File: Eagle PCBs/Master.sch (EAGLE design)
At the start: 12 parts

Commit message: Master PCB WIP
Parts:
- removed C4: 22uF 16V, rcl:C-EU025-025X050
- removed LED, SLAVE_PWR: (no value), con-molex:KK-156-2
- removed LED_T: BD239, transistor-neu-to92:BD239
- removed SLAVE_DATA: (no value), con-molex:22-23-2061
- added R1: 120Ω, rcl:R-EU_0207/10
- added SLAVE: 212528-0801, SamacSys_Parts:212528-0801
- 5V-VRR: value 7805T -> L7805CV
- C1: value 220uF 16V -> 0.33uF
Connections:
- removed net 12VCC: 5V-VRR.VI, C1.1, C2.1, LED-1.S, PSU.2, SLAVE_PWR-1.S
- removed net LED_DIM: LED_T.B
- removed net LED_GND: LED-2.S, LED_T.C
- new net VDD: 5V-VRR.VO, C2.1, C3.1, MEGA-1.S
- net GND: now also SLAVE.7; no longer C4.2, LED_T.E, SLAVE_PWR-2.S
- net MEGA_P18: now also MEGA-5.S; no longer MEGA-4.S
- net MEGA_P19: now also MEGA-3.S; no longer MEGA-5.S
- net MEGA_P2: now also MEGA-4.S; no longer MEGA-3.S
- net RS485_A: now also R1.2, SLAVE.3; no longer SLAVE_DATA-1.S
- net RS485_B: now also R1.1, SLAVE.4; no longer SLAVE_DATA-2.S
- net VCC: now also 5V-VRR.VI, C1.1, PSU.2, SLAVE.8; no longer 5V-VRR.VO, C3.1, C4.1, MEGA-1.S
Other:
- note added: "12 to 5V, 1.5A"
- note added: "Arduino Mega Connection"
- note added: "Slave Connection"
- note removed: "12 to 5V, 1A https://www.eleccircuit.com/12v-to-5v-converter-step-down-3a-regulator/"
- note removed: "Arduino Mega Connections"
- note removed: "LED Dimmer"
- note removed: "RS-485 Slave Connections"
- moved on the sheet: C1, C2, C3, MEGA-1, MEGA-2, MEGA-3, MEGA-4, MEGA-5, MEGA-6, PSU

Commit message: Master PCB WIP
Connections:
- removed net VDD: 5V-VRR.VO, C2.1, C3.1, MEGA-1.S
- new net VCC12: 5V-VRR.VI, C1.1, PSU.2, SLAVE.8
- net GND: now also RS485-MASTERP.GND
- net VCC: now also 5V-VRR.VO, C2.1, C3.1, MEGA-1.S, RS485-MASTERP.VCC; no longer 5V-VRR.VI, C1.1, PSU.2, SLAVE.8
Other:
- moved on the sheet: C3, MEGA-1, MEGA-2, MEGA-3, MEGA-4, MEGA-5, MEGA-6
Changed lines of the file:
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@@
 <attribute name="VALUE" x="106.68" y="40.64" size="1.778" layer="96"/>
 </instance>
-<instance part="MEGA" gate="-1" x="116.84" y="27.94" smashed="yes">
-<attribute name="NAME" x="119.38" y="27.178" size="1.524" layer="95"/>
-<attribute name="VALUE" x="116.078" y="29.337" size="1.778" layer="96"/>
-</instance>
-<instance part="MEGA" gate="-2" x="116.84" y="25.4" smashed="yes">
+<instance part="MEGA" gate="-1" x="116.84" y="25.4" smashed="yes">
 <attribute name="NAME" x="119.38" y="24.638" size="1.524" layer="95"/>
-</instance>
-<instance part="MEGA" gate="-3" x="116.84" y="22.86" smashed="yes">
+<attribute name="VALUE" x="116.078" y="26.797" size="1.778" layer="96"/>
+</instance>
+<instance part="MEGA" gate="-2" x="116.84" y="22.86" smashed="yes">
 <attribute name="NAME" x="119.38" y="22.098" size="1.524" layer="95"/>
 </instance>
-<instance part="MEGA" gate="-4" x="116.84" y="20.32" smashed="yes">
+<instance part="MEGA" gate="-3" x="116.84" y="20.32" smashed="yes">
 <attribute name="NAME" x="119.38" y="19.558" size="1.524" layer="95"/>
 </instance>
-<instance part="MEGA" gate="-5" x="116.84" y="17.78" smashed="yes">
+<instance part="MEGA" gate="-4" x="116.84" y="17.78" smashed="yes">
 <attribute name="NAME" x="119.38" y="17.018" size="1.524" layer="95"/>
 </instance>
-<instance part="MEGA" gate="-6" x="116.84" y="15.24" smashed="yes">
+<instance part="MEGA" gate="-5" x="116.84" y="15.24" smashed="yes">
 <attribute name="NAME" x="119.38" y="14.478" size="1.524" layer="95"/>
+</instance>
+<instance part="MEGA" gate="-6" x="116.84" y="12.7" smashed="yes">
+<attribute name="NAME" x="119.38" y="11.938" size="1.524" layer="95"/>
 </instance>
 <instance part="PSU" gate="G$1" x="7.62" y="17.78" smashed="yes">
@@
 <attribute name="VALUE" x="64.77" y="22.86" size="1.778" layer="96" align="center-left"/>
 </instance>
-<instance part="C3" gate="G$1" x="134.62" y="40.64" smashed="yes">
-<attribute name="NAME" x="136.144" y="41.021" size="1.778" layer="95"/>
-<attribute name="VALUE" x="136.144" y="35.941" size="1.778" layer="96"/>
+<instance part="C3" gate="G$1" x="139.7" y="35.56" smashed="yes">
+<attribute name="NAME" x="141.224" y="35.941" size="1.778" layer="95"/>
+<attribute name="VALUE" x="141.224" y="30.861" size="1.778" layer="96"/>
 </instance>
 <instance part="R1" gate="G$1" x="149.86" y="55.88" smashed="yes" rot="R270">
 <attribute name="NAME" x="151.3586" y="59.69" size="1.778" layer="95" rot="R270"/>
 <attribute name="VALUE" x="146.558" y="59.69" size="1.778" layer="96" rot="R270"/>
+</instance>
+<instance part="RS485-MASTER" gate="P" x="116.84" y="35.56" smashed="yes" rot="R90">
+<attribute name="NAME" x="117.602" y="34.798" size="1.778" layer="95" rot="R180"/>
 </instance>
 </instances>
@@
 </busses>
 <nets>
-<net name="VCC" class="0">
+<net name="VCC12" class="0">
 <segment>
 <pinref part="5V-VRR" gate="A1" pin="VI"/>
@@
 </segment>
 </net>
-<net name="VDD" class="0">
+<net name="VCC" class="0">
 <segment>
 <pinref part="5V-VRR" gate="A1" pin="VO"/>
@@
 <segment>
 <pinref part="MEGA" gate="-1" pin="S"/>
-<wire x1="114.3" y1="27.94" x2="106.68" y2="27.94" width="0.1524" layer="91"/>
-<label x="114.3" y="27.94" size="1.778" layer="95" rot="R180"/>
+<wire x1="114.3" y1="25.4" x2="106.68" y2="25.4" width="0.1524" layer="91"/>
+<label x="114.3" y="25.4" size="1.778" layer="95" rot="R180"/>
 </segment>
 <segment>
 <pinref part="C3" gate="G$1" pin="1"/>
-<wire x1="134.62" y1="43.18" x2="134.62" y2="45.72" width="0.1524" layer="91"/>
-<label x="134.62" y="45.72" size="1.778" layer="95"/>
+<wire x1="139.7" y1="38.1" x2="139.7" y2="40.64" width="0.1524" layer="91"/>
+<label x="139.7" y="40.64" size="1.778" layer="95"/>
+</segment>
+<segment>
+<pinref part="RS485-MASTER" gate="P" pin="VCC"/>
+<wire x1="109.22" y1="35.56" x2="106.68" y2="35.56" width="0.1524" layer="91"/>
+<label x="104.14" y="35.56" size="1.778" layer="95"/>
 </segment>
 </net>
@@
 <segment>
 <pinref part="MEGA" gate="-2" pin="S"/>
-<wire x1="114.3" y1="25.4" x2="106.68" y2="25.4" width="0.1524" layer="91"/>
-<label x="114.3" y="25.4" size="1.778" layer="95" rot="R180"/>
+<wire x1="114.3" y1="22.86" x2="106.68" y2="22.86" width="0.1524" layer="91"/>
+<label x="114.3" y="22.86" size="1.778" layer="95" rot="R180"/>
 </segment>
 <segment>
@@
 <segment>
 <pinref part="C3" gate="G$1" pin="2"/>
-<wire x1="134.62" y1="35.56" x2="134.62" y2="30.48" width="0.1524" layer="91"/>
-<label x="134.62" y="30.48" size="1.778" layer="95"/>
+<wire x1="139.7" y1="30.48" x2="139.7" y2="25.4" width="0.1524" layer="91"/>
+<label x="139.7" y="25.4" size="1.778" layer="95"/>
 </segment>
 <segment>
@@
 <wire x1="68.58" y1="15.24" x2="78.74" y2="15.24" width="0.1524" layer="91"/>
 <label x="71.12" y="15.24" size="1.778" layer="95"/>
+</segment>
+<segment>
+<pinref part="RS485-MASTER" gate="P" pin="GND"/>
+<wire x1="124.46" y1="35.56" x2="127" y2="35.56" width="0.1524" layer="91"/>
+<label x="124.46" y="35.56" size="1.778" layer="95"/>
 </segment>
 </net>
@@
 <segment>
 <pinref part="MEGA" gate="-4" pin="S"/>
-<wire x1="114.3" y1="20.32" x2="106.68" y2="20.32" width="0.1524" layer="91"/>
-<label x="114.3" y="20.32" size="1.778" layer="95" rot="R180"/>
+<wire x1="114.3" y1="17.78" x2="106.68" y2="17.78" width="0.1524" layer="91"/>
+<label x="114.3" y="17.78" size="1.778" layer="95" rot="R180"/>
 </segment>
 </net>
@@
 <segment>
 <pinref part="MEGA" gate="-3" pin="S"/>
-<wire x1="114.3" y1="22.86" x2="106.68" y2="22.86" width="0.1524" layer="91"/>
-<label x="114.3" y="22.86" size="1.778" layer="95" rot="R180"/>
+<wire x1="114.3" y1="20.32" x2="106.68" y2="20.32" width="0.1524" layer="91"/>
+<label x="114.3" y="20.32" size="1.778" layer="95" rot="R180"/>
 </segment>
 </net>
@@
 <segment>
 <pinref part="MEGA" gate="-5" pin="S"/>
-<wire x1="114.3" y1="17.78" x2="106.68" y2="17.78" width="0.1524" layer="91"/>
-<label x="114.3" y="17.78" size="1.778" layer="95" rot="R180"/>
+<wire x1="114.3" y1="15.24" x2="106.68" y2="15.24" width="0.1524" layer="91"/>
+<label x="114.3" y="15.24" size="1.778" layer="95" rot="R180"/>
 </segment>
 </net>
@@
 </sheet>
 </sheets>
+<errors>
+</errors>
 </schematic>
 </drawing>

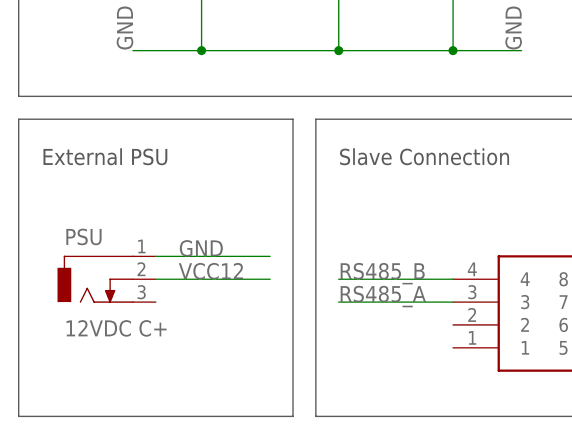
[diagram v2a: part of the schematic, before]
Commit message: Updated DC Barrel Jack
DC-044A
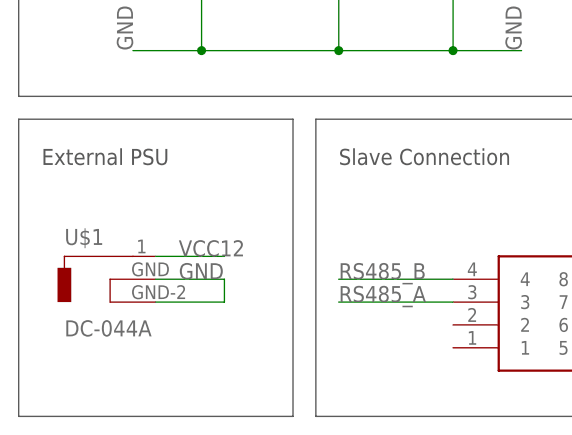
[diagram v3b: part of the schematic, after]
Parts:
- removed PSU: 12VDC C+, con-jack:DCJ0202
- added U$1: DC-044A, A10 Library:DC-044A
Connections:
- net GND: now also U$1.GND, U$1.GND-2; no longer PSU.1
- net VCC12: now also U$1.1; no longer PSU.2
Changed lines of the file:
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@@
 <part name="RS485-MASTER" library="A10 Library" deviceset="MAX487CPA" device="" package3d_urn="urn:adsk.eagle:package:29519/2"/>
 <part name="MEGA" library="con-molex" library_urn="urn:adsk.eagle:library:165" deviceset="22-23-2061" device="" package3d_urn="urn:adsk.eagle:package:8078637/1"/>
-<part name="PSU" library="con-jack" library_urn="urn:adsk.eagle:library:154" deviceset="DCJ0202" device="" package3d_urn="urn:adsk.eagle:package:7491/1" value="12VDC C+"/>
 <part name="5V-VRR" library="linear" library_urn="urn:adsk.eagle:library:262" deviceset="78*" device="T" package3d_urn="urn:adsk.eagle:package:16414/1" technology="05" value="L7805CV"/>
 <part name="C1" library="rcl" library_urn="urn:adsk.eagle:library:334" deviceset="C-EU" device="025-025X050" package3d_urn="urn:adsk.eagle:package:23629/2" value="0.33uF"/>
@@
 <part name="C3" library="rcl" library_urn="urn:adsk.eagle:library:334" deviceset="C-EU" device="025-025X050" package3d_urn="urn:adsk.eagle:package:23629/2" value="0.1uF"/>
 <part name="R1" library="rcl" library_urn="urn:adsk.eagle:library:334" deviceset="R-EU_" device="0207/10" package3d_urn="urn:adsk.eagle:package:23491/2" value="120Ω"/>
+<part name="U$1" library="A10 Library" deviceset="DC-044A" device=""/>
 </parts>
 <sheets>
@@
 <attribute name="NAME" x="119.38" y="11.938" size="1.524" layer="95"/>
 </instance>
-<instance part="PSU" gate="G$1" x="7.62" y="17.78" smashed="yes">
-<attribute name="NAME" x="5.08" y="21.59" size="1.778" layer="95"/>
-<attribute name="VALUE" x="5.08" y="11.43" size="1.778" layer="96"/>
-</instance>
 <instance part="5V-VRR" gate="A1" x="35.56" y="66.04" smashed="yes">
 <attribute name="NAME" x="27.94" y="71.755" size="1.778" layer="95"/>
@@
 <attribute name="NAME" x="117.602" y="34.798" size="1.778" layer="95" rot="R180"/>
 </instance>
+<instance part="U$1" gate="G$1" x="10.16" y="15.24" smashed="yes">
+<attribute name="NAME" x="5.08" y="21.59" size="1.778" layer="95"/>
+<attribute name="VALUE" x="5.08" y="11.43" size="1.778" layer="96"/>
+</instance>
 </instances>
 <busses>
@@
 </segment>
 <segment>
-<pinref part="PSU" gate="G$1" pin="2"/>
-<wire x1="15.24" y1="17.78" x2="27.94" y2="17.78" width="0.1524" layer="91"/>
-<label x="17.78" y="17.78" size="1.778" layer="95"/>
-</segment>
-<segment>
 <pinref part="SLAVE" gate="G$1" pin="8"/>
 <wire x1="68.58" y1="17.78" x2="78.74" y2="17.78" width="0.1524" layer="91"/>
 <label x="71.12" y="17.78" size="1.778" layer="95"/>
+</segment>
+<segment>
+<wire x1="15.24" y1="20.32" x2="22.86" y2="20.32" width="0.1524" layer="91"/>
+<label x="17.78" y="20.32" size="1.778" layer="95"/>
+<pinref part="U$1" gate="G$1" pin="1"/>
 </segment>
 </net>
@@
 </segment>
 <segment>
-<pinref part="PSU" gate="G$1" pin="1"/>
-<wire x1="15.24" y1="20.32" x2="27.94" y2="20.32" width="0.1524" layer="91"/>
-<label x="17.78" y="20.32" size="1.778" layer="95"/>
-</segment>
-<segment>
 <pinref part="C3" gate="G$1" pin="2"/>
 <wire x1="139.7" y1="30.48" x2="139.7" y2="25.4" width="0.1524" layer="91"/>
@@
 <label x="124.46" y="35.56" size="1.778" layer="95"/>
 </segment>
+<segment>
+<wire x1="15.24" y1="15.24" x2="22.86" y2="15.24" width="0.1524" layer="91"/>
+<wire x1="15.24" y1="17.78" x2="22.86" y2="17.78" width="0.1524" layer="91"/>
+<wire x1="22.86" y1="15.24" x2="22.86" y2="17.78" width="0.1524" layer="91"/>
+<label x="17.78" y="17.78" size="1.778" layer="95"/>
+<pinref part="U$1" gate="G$1" pin="GND"/>
+<pinref part="U$1" gate="G$1" pin="GND-2"/>
+</segment>
 </net>
